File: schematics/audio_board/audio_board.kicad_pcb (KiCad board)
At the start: 2 copper layers, 50 x 50 mm, 66 parts, among them J1 servo ctrl, J10 charge en, J3 power, J4 pyr ctrl, J5 servo out, J6 pyr in, J7 audio ctrl, J8 speaker, J9 battery, Q1 bc847, Q2 bc847, Q7 dgm2305ux, Q8 dgm2305ux, U1 TPS613222ADBV, U3 TPS613222ADBV, U4 TPS613222ADBV, U5 PAM8302AAD, U8 MCP73812

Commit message: Placing parts onto PCB...
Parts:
- removed C12, C17, C20: 100n, Capacitor_SMD:C_0603_1608Metric_Pad1.08x0.95mm_HandSolder
- removed D1, D3: 1N5819, Diode_THT:D_DO-41_SOD81_P7.62mm_Horizontal
- removed D4, D5, D6, D7: LED, LED_THT:LED_D5.0mm
- removed J10: charge en, Connector_PinSocket_2.54mm:PinSocket_1x02_P2.54mm_Vertical
- removed J5: servo out, Connector_PinSocket_2.54mm:PinSocket_1x03_P2.54mm_Vertical
- removed J9: battery, Connector_PinSocket_2.54mm:PinSocket_1x02_P2.54mm_Vertical
- removed L2: 4.7uH, Inductor_SMD:L_1008_2520Metric
- removed Q8: dgm2305ux, Package_TO_SOT_SMD:SOT-23
- removed R10, R12, R13, R14, R4: 1k, Capacitor_SMD:C_0603_1608Metric_Pad1.08x0.95mm_HandSolder
- removed R21: 100k, Resistor_SMD:R_0603_1608Metric_Pad0.98x0.95mm_HandSolder
- removed R83: 2k, Capacitor_SMD:C_0603_1608Metric_Pad1.08x0.95mm_HandSolder
- removed U8: MCP73812, Package_TO_SOT_SMD:SOT-23-5
- added C16: 4u7, Capacitor_SMD:C_0603_1608Metric, F.Cu at (24.2, 37.3)
- added C21: 100n, Capacitor_SMD:C_0603_1608Metric, F.Cu at (24.2, 39.8)
- added C22: 100n, Capacitor_SMD:C_0603_1608Metric, F.Cu at (24.2, 42.3)
- added C23: 22u, Capacitor_SMD:C_0603_1608Metric_Pad1.08x0.95mm_HandSolder, F.Cu at (33.5, 37.3)
- added C24: 100n, Capacitor_SMD:C_0603_1608Metric, F.Cu at (24.2, 44.8)
- added C25: 22u, Capacitor_SMD:C_0603_1608Metric_Pad1.08x0.95mm_HandSolder, F.Cu at (33.5, 39.8)
- added C26: 100n, Capacitor_SMD:C_0603_1608Metric, F.Cu at (24.2, 47.3)
- added C27: 100n, Capacitor_SMD:C_0603_1608Metric, F.Cu at (24.2, 49.9)
- added C3: 22u, Capacitor_SMD:C_0603_1608Metric_Pad1.08x0.95mm_HandSolder, F.Cu at (66.0, 115.3)
- added J2: mic, Connector_PinSocket_2.54mm:PinSocket_1x02_P2.54mm_Vertical, F.Cu at (33.6, 50.9)
- added Q3: dgm2305ux, Package_TO_SOT_SMD:SOT-23, F.Cu at (63.1, 116.5)
- added R15: 1k, Capacitor_SMD:C_0603_1608Metric_Pad1.08x0.95mm_HandSolder, F.Cu at (59.1, 111.1)
- added R16: 100k, Resistor_SMD:R_0603_1608Metric_Pad0.98x0.95mm_HandSolder, F.Cu at (60.1, 116.4)
- added R18: 100k, Resistor_SMD:R_0603_1608Metric_Pad0.98x0.95mm_HandSolder, F.Cu at (33.5, 42.3)
- added R19: 100k, Resistor_SMD:R_0603_1608Metric_Pad0.98x0.95mm_HandSolder, F.Cu at (33.5, 44.8)
- added R22: 2k2, Resistor_SMD:R_0603_1608Metric_Pad0.98x0.95mm_HandSolder, F.Cu at (33.5, 47.3)
- added R23: 33k, Capacitor_SMD:C_0603_1608Metric_Pad1.08x0.95mm_HandSolder, F.Cu at (37.8, 37.3)
- added R24: 100k, Resistor_SMD:R_0603_1608Metric_Pad0.98x0.95mm_HandSolder, F.Cu at (37.8, 39.8)
- added R25: 100k, Resistor_SMD:R_0603_1608Metric_Pad0.98x0.95mm_HandSolder, F.Cu at (71.8, 55.3)
- added R27: 2k2, Resistor_SMD:R_0603_1608Metric_Pad0.98x0.95mm_HandSolder, F.Cu at (37.8, 44.8)
- added R28: 2k2, Resistor_SMD:R_0603_1608Metric_Pad0.98x0.95mm_HandSolder, F.Cu at (37.8, 47.3)
- added R29: 33k, Capacitor_SMD:C_0603_1608Metric_Pad1.08x0.95mm_HandSolder, F.Cu at (42.2, 37.3)
- added R30: 2k2, Resistor_SMD:R_0603_1608Metric_Pad0.98x0.95mm_HandSolder, F.Cu at (42.2, 39.8)
- added R31: 1k, Capacitor_SMD:C_0603_1608Metric_Pad1.08x0.95mm_HandSolder, F.Cu at (42.2, 42.3)
- added R32: 100k, Resistor_SMD:R_0603_1608Metric_Pad0.98x0.95mm_HandSolder, F.Cu at (42.2, 44.8)
- added R33: 100k, Resistor_SMD:R_0603_1608Metric_Pad0.98x0.95mm_HandSolder, F.Cu at (59.5, 70.2)
- added U2: MCP1802x-xx02xOT, Package_TO_SOT_SMD:SOT-23-5, F.Cu at (72.9, 116.4)
- added U6: TLV9061xDBV, Package_TO_SOT_SMD:SOT-23-5, F.Cu at (28.7, 43.1)
- added U7: TLV9061xDBV, Package_TO_SOT_SMD:SOT-23-5, F.Cu at (28.7, 47.7)
- C15: value 22u -> 100n; footprint Capacitor_SMD:C_0603_1608Metric_Pad1.08x0.95mm_HandSolder -> Capacitor_SMD:C_0603_1608Metric
- C4, C5: value 22u -> 4u7; footprint Capacitor_SMD:C_0603_1608Metric_Pad1.08x0.95mm_HandSolder -> Capacitor_SMD:C_0603_1608Metric
- C7, C8: footprint Capacitor_SMD:C_0603_1608Metric_Pad1.08x0.95mm_HandSolder -> Capacitor_SMD:C_0603_1608Metric
- C9: value 100n -> 4u7; footprint Capacitor_SMD:C_0603_1608Metric_Pad1.08x0.95mm_HandSolder -> Capacitor_SMD:C_0603_1608Metric
- J1: value servo ctrl -> pyr ctrl
- R1: value 100k -> 2k; footprint Resistor_SMD:R_0603_1608Metric_Pad0.98x0.95mm_HandSolder -> Capacitor_SMD:C_0603_1608Metric_Pad1.08x0.95mm_HandSolder
- R17: value 2k -> 1k
- R20: value 100k -> 2k2
- R7: value 33 -> 100k
- R8: value 1k -> 100k; footprint Capacitor_SMD:C_0603_1608Metric_Pad1.08x0.95mm_HandSolder -> Resistor_SMD:R_0603_1608Metric_Pad0.98x0.95mm_HandSolder
- U3: value TPS613222ADBV -> MCP1802x-xx02xOT
- moved C15 68.0 mm to (47.3, 139.5)
- moved C9 68.0 mm to (35.1, 136.6)
- moved R20 68.0 mm to (40.2, 136.8)
- moved R26 64.2 mm to (59.1, 113.1)
- moved J3 53.8 mm to (53.0, 64.5)
- moved R17 43.2 mm to (58.1, 116.3)
- moved R3 39.3 mm to (94.1, 69.1), turned to 90 degrees
- moved R1 37.5 mm to (74.5, 54.4)
- moved U3 37.2 mm to (82.6, 116.5)
- moved Q1 36.7 mm to (63.1, 112.1)
- moved R7 36.7 mm to (94.1, 73.1), turned to 90 degrees
- moved C8 36.4 mm to (85.8, 116.7), turned to -90 degrees
- moved C5 36.3 mm to (69.5, 116.7)
- moved C4 35.8 mm to (76.0, 116.7), turned to -90 degrees
- moved D2 33.3 mm to (64.0, 64.0), turned to 180 degrees
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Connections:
- net /pwr+ renamed Net-(D2-A)
- C15 pad 1: /Power ctrl/pwr_out -> /Vdd_mic
- C4 pad 1: /Vin -> /Vdd_mic
- C5 pad 1: /5V_servo -> /pwr_mic
- C7 pad 1: /power -> /pwr_mic
- C8 pad 1: /Vbatt -> /Vbias_mic
- C9 pad 1: /5V_servo -> Net-(C23-Pad2)
- C9 pad 2: GND -> Net-(U7-+)
- J1 pad 1: /Power ctrl/en -> /mic_en
- J1 pad 3: Net-(J1-Pin_3) -> /mic_to_adc
- Q7 pad 2: /Power ctrl/pwr_out -> /Vin
- Q7 pad 3: /5V_servo -> /Power ctrl PYR/pwr_out
- R1 pad 1: /charge_en -> /audio_in
- R1 pad 2: GND -> /audio_dac
- R11 pad 1: Net-(Q8-G) -> Net-(Q7-G)
- R17 pad 1: GND -> Net-(Q3-G)
- R17 pad 2: Net-(J4-Pin_3) -> Net-(Q1-C)
- R2 pad 1: /audio_dac -> GND
- R20 pad 1: /Power ctrl/en -> Net-(U6--)
- R20 pad 2: GND -> /Vdd_mic
- R26 pad 2: /audio_en -> /mic_en
- R3 pad 1: GND -> /pyr_in
- R3 pad 2: /audio_dac -> /5V_pyr
- R6 pad 2: Net-(Q8-G) -> Net-(Q7-G)
- R7 pad 1: Net-(J1-Pin_3) -> Net-(R7-Pad1)
- R7 pad 2: Net-(J5-Pin_3) -> /pyr_in
- R8 pad 1: /Power ctrl/en -> GND
- R8 pad 2: Net-(Q1-B) -> Net-(R7-Pad1)
- R9 pad 1: /5V_servo -> GND
- R9 pad 2: Net-(Q7-G) -> /audio_en
- U3 pad 1: Net-(U3-SW) -> /pwr_mic
- U3 pad 3: unconnected-(U3-NC-Pad3) -> /pwr_mic
- U3 pad 4: /5V_servo -> unconnected-(U3-NC-Pad4)
- U3 pad 5: unconnected-(U3-NC-Pad5) -> /Vbias_mic
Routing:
- net GND: track 338.4 -> 0.00 mm, vias 13 -> 0
- net /Vin: track 87.3 -> 0.00 mm, vias 4 -> 0
- net /Vbatt: track 56.2 -> 0.00 mm
- net /pyr_in: track 48.2 -> 0.00 mm, vias 2 -> 0
- net Net-(J5-Pin_3): track 43.8 -> 0.00 mm, vias 2 -> 0
- net /5V_audio: track 43.7 -> 0.00 mm, vias 1 -> 0
- net /5V_servo: track 36.6 -> 0.00 mm
- net /audio_en: track 34.7 -> 0.00 mm
- net /Power ctrl/en: track 30.4 -> 0.00 mm
- net /5V_pyr: track 27.6 -> 0.00 mm, vias 1 -> 0
- net Net-(D2-A): track 24.6 -> 0.00 mm
- net /audio_dac: track 23.8 -> 0.00 mm
- net /Power ctrl/pwr_out: track 15.1 -> 0.00 mm, vias 1 -> 0
- net /charge_en: track 15.1 -> 0.00 mm
- net /pyr_en: track 14.2 -> 0.00 mm
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
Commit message: a
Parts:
- moved C22 117.4 mm to (76.2, 147.5)
- moved C25 115.0 mm to (91.0, 139.4), turned to 90 degrees
- moved C26 113.4 mm to (85.8, 142.5), turned to 180 degrees
- moved R29 112.3 mm to (89.0, 139.4), turned to 90 degrees
- moved C23 111.9 mm to (77.0, 140.4), turned to 90 degrees
- moved R24 111.2 mm to (83.0, 141.4), turned to 90 degrees
- moved R31 111.1 mm to (46.0, 153.4)
- moved C24 111.1 mm to (28.0, 155.9)
- moved J2 111.1 mm to (37.5, 162.0)
- moved R27 111.1 mm to (41.7, 155.9)
- moved C27 111.1 mm to (28.0, 160.9)
- moved R28 111.1 mm to (41.7, 158.4)
- moved C16 110.5 mm to (66.2, 139.5)
- moved R23 109.6 mm to (75.0, 140.4), turned to 90 degrees
- moved C21 108.2 mm to (71.8, 137.0)
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
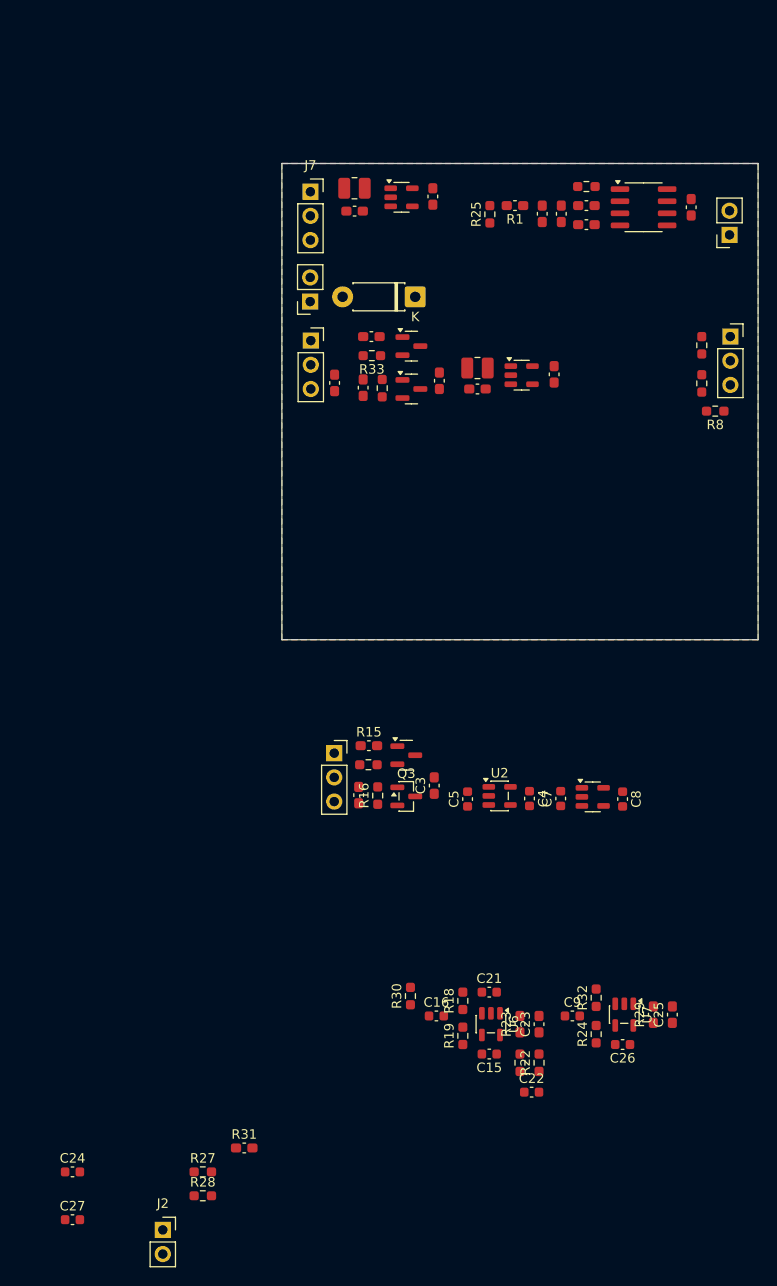
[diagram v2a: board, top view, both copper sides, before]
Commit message: It passes, board seems to be at least logically done. Other than it is 2-layers board and is not quite up to best practices, it is done. May be declare it good enough?
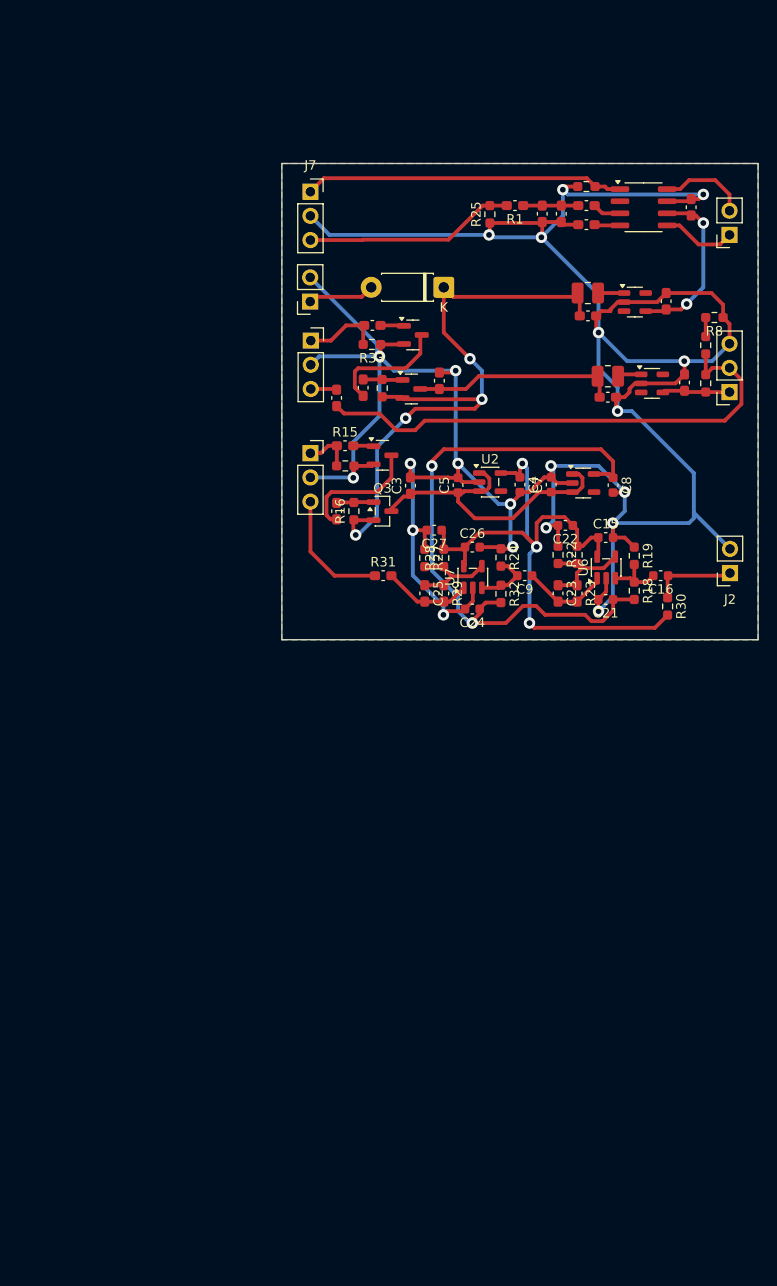
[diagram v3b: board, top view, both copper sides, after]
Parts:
- moved J2 91.1 mm to (97.0, 93.0), turned to 180 degrees
- moved C27 81.7 mm to (66.0, 88.5), turned to 180 degrees
- moved C24 72.5 mm to (70.0, 96.8), turned to 180 degrees
- moved R28 71.6 mm to (67.0, 91.4), turned to 90 degrees
- moved R27 68.5 mm to (65.0, 91.4), turned to -90 degrees
- moved R31 61.8 mm to (60.6, 93.3)
- moved C22 59.6 mm to (79.8, 88.0), turned to 180 degrees
- moved C15 55.6 mm to (84.0, 89.3), turned to 0 degrees
- moved C26 54.6 mm to (70.0, 90.3), turned to 0 degrees
- moved R20 53.7 mm to (81.0, 91.1), turned to 90 degrees
- moved R19 53.5 mm to (87.0, 91.2), turned to -90 degrees
- moved R22 53.4 mm to (79.0, 91.1), turned to -90 degrees
- moved C16 51.9 mm to (89.8, 93.3), turned to 180 degrees
- moved C25 51.3 mm to (65.0, 95.1), turned to -90 degrees
- moved R24 51.0 mm to (73.0, 91.4), turned to -90 degrees
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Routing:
- net GND: track 0.00 -> 332.2 mm, vias 0 -> 21
- net /Vin: track 0.00 -> 68.5 mm, vias 0 -> 4
- net /Vbias_mic: track 0.00 -> 67.5 mm, vias 0 -> 2
- net /Vdd_mic: track 0.00 -> 65.9 mm, vias 0 -> 3
- net /pyr_in: track 0.00 -> 54.0 mm
- net /audio_en: track 0.00 -> 33.6 mm
- net /pwr_mic: track 0.00 -> 32.0 mm
- net /audio_dac: track 0.00 -> 22.1 mm
- net /Power ctrl PYR/pwr_out: track 0.00 -> 21.5 mm
- net /5V_audio: track 0.00 -> 18.1 mm, vias 0 -> 2
- net Net-(Q1-C): track 0.00 -> 13.2 mm
- net /mic_to_adc: track 0.00 -> 13.1 mm
- net Net-(Q2-C): track 0.00 -> 12.6 mm
- net Net-(U6--): track 0.00 -> 10.7 mm
- net Net-(U7--): track 0.00 -> 10.2 mm
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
